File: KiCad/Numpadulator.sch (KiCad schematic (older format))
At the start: 1 part, among them U1 PRO_MICRO_C

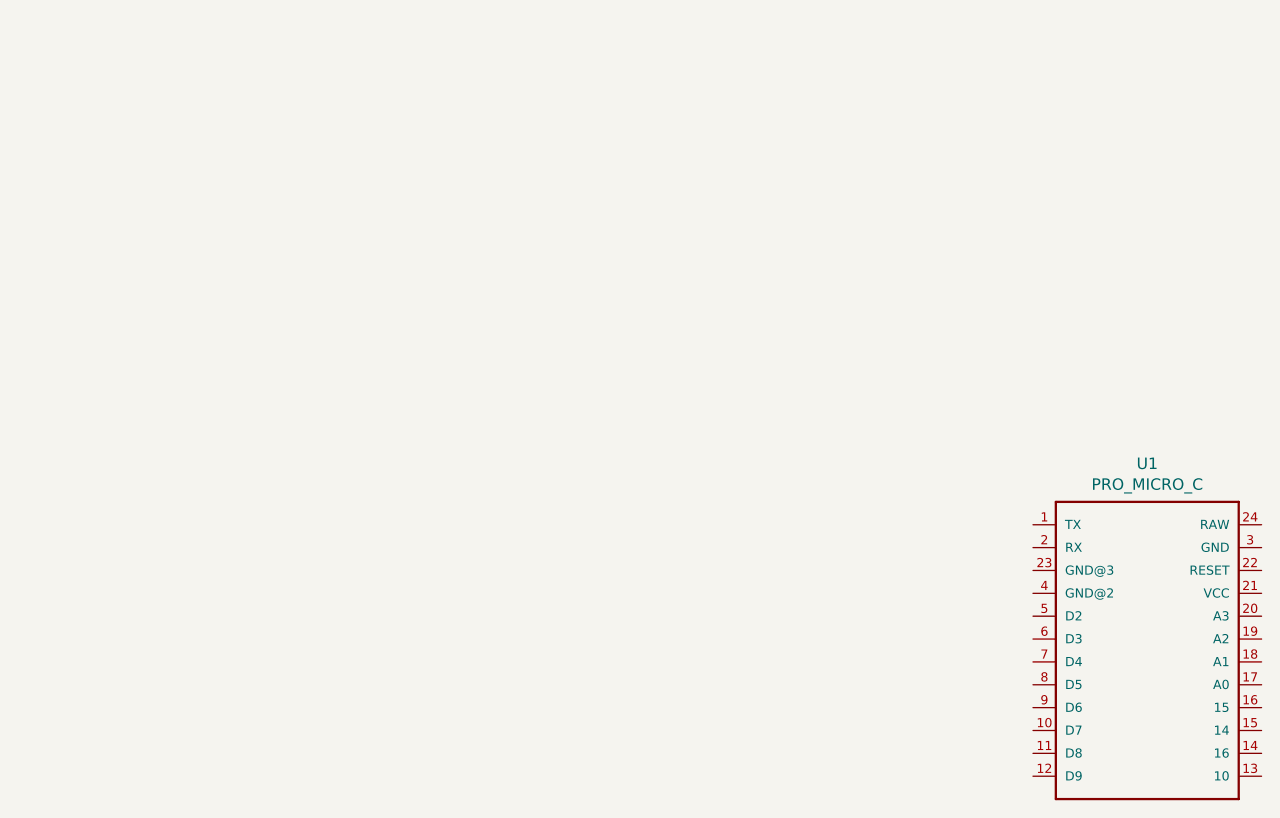
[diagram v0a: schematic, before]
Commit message: Dropped in RotEnc and hooked up OLED
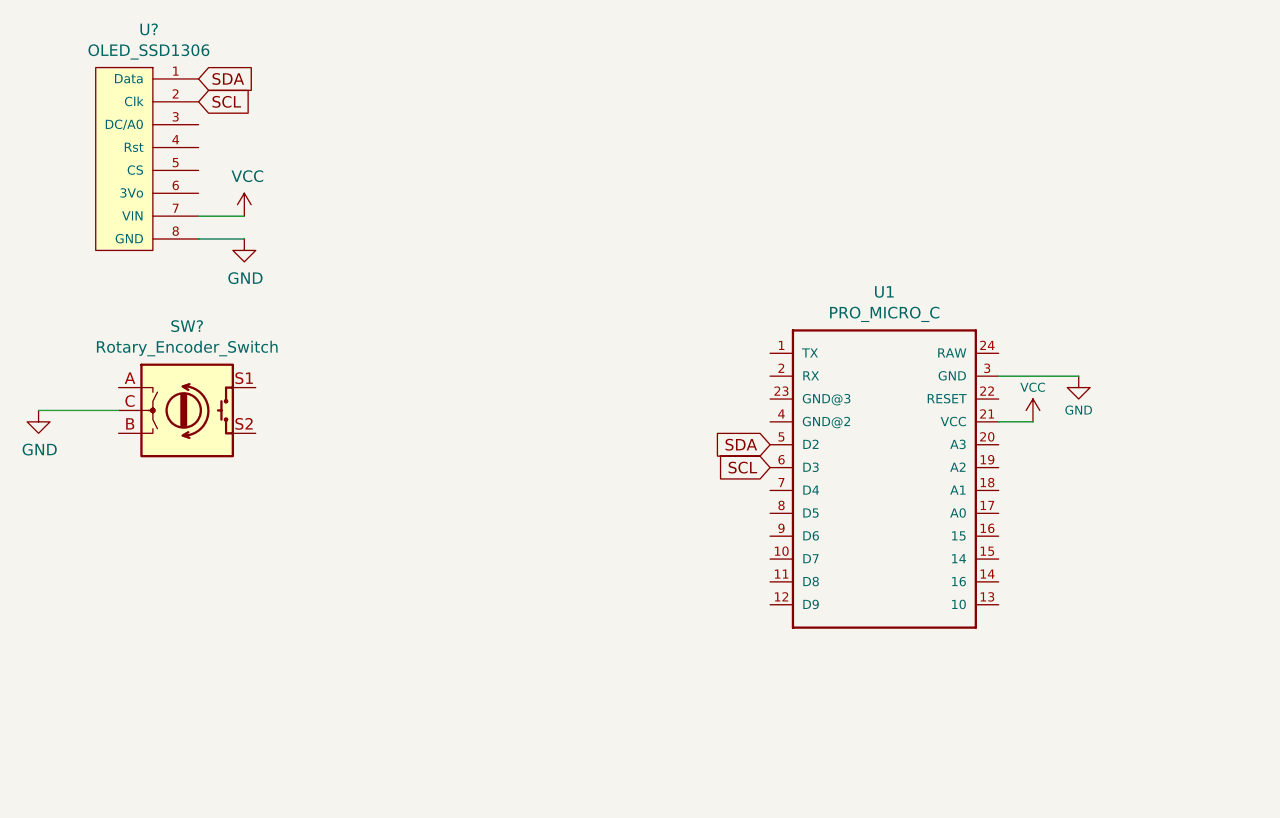
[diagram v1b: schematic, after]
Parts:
- added SW?: Rotary_Encoder_Switch, symbol Device:Rotary_Encoder_Switch
- added U?: OLED_SSD1306, symbol Custom_Library:OLED_SSD1306
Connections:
- net VCC: now reaches U1.21 (VCC)
- net VCC: now also U?.7 (VIN)
- net GND: now reaches U1.3 (GND)
- net GND: now also SW?.C, U?.8 (GND)
- net SDA: now reaches U1.5 (D2)
- net SDA: now also U?.1 (Data)
- net SCL: now reaches U1.6 (D3)
- net SCL: now also U?.2 (Clk)
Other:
- moved on the sheet: U1
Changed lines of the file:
@@
 L PRO_MICRO_C:PRO_MICRO_C U1
 U 1 1 5F1B84A1
-P 5600 3350
-F 0 "U1" H 5600 4117 50  0000 C CNN
-F 1 "PRO_MICRO_C" H 5600 4026 50  0000 C CNN
-F 2 "SparkFun-Boards:PRO_MICRO_C" H 5600 3350 50  0001 L BNN
-F 3 "" H 5600 3350 50  0001 C CNN
-	1    5600 3350
+P 4450 2600
+F 0 "U1" H 4450 3367 50  0000 C CNN
+F 1 "PRO_MICRO_C" H 4450 3276 50  0000 C CNN
+F 2 "SparkFun-Boards:PRO_MICRO_C" H 4450 2600 50  0001 L BNN
+F 3 "" H 4450 2600 50  0001 C CNN
+	1    4450 2600
 	1    0    0    -1
 $EndComp
+$Comp
+L Device:Rotary_Encoder_Switch SW?
+U 1 1 5F1D3156
+P 1400 2350
+F 0 "SW?" H 1400 2717 50  0000 C CNN
+F 1 "Rotary_Encoder_Switch" H 1400 2626 50  0000 C CNN
+F 2 "" H 1250 2510 50  0001 C CNN
+F 3 "~" H 1400 2610 50  0001 C CNN
+	1    1400 2350
+	1    0    0    -1
+$EndComp
+$Comp
+L Custom_Library:OLED_SSD1306 U?
+U 1 1 5F1EF454
+P 1100 1250
+F 0 "U?" V 535 1383 50  0000 C CNN
+F 1 "OLED_SSD1306" V 626 1383 50  0000 C CNN
+F 2 "" H 1150 1725 50  0001 C CNN
+F 3 "" H 1150 1725 50  0001 C CNN
+	1    1100 1250
+	0    1    1    0
+$EndComp
+Text GLabel 1450 900  2    50   Input ~ 0
+SDA
+Text GLabel 1450 1000 2    50   Input ~ 0
+SCL
+Text GLabel 3950 2500 0    50   Input ~ 0
+SDA
+Text GLabel 3950 2600 0    50   Input ~ 0
+SCL
+$Comp
+L power:VCC #PWR?
+U 1 1 5F1F5638
+P 1650 1500
+F 0 "#PWR?" H 1650 1350 50  0001 C CNN
+F 1 "VCC" H 1665 1673 50  0000 C CNN
+F 2 "" H 1650 1500 50  0001 C CNN
+F 3 "" H 1650 1500 50  0001 C CNN
+	1    1650 1500
+	1    0    0    -1
+$EndComp
+$Comp
+L power:GND #PWR?
+U 1 1 5F1F5EDF
+P 1650 1600
+F 0 "#PWR?" H 1650 1350 50  0001 C CNN
+F 1 "GND" H 1655 1427 50  0000 C CNN
+F 2 "" H 1650 1600 50  0001 C CNN
+F 3 "" H 1650 1600 50  0001 C CNN
+	1    1650 1600
+	1    0    0    -1
+$EndComp
+Wire Wire Line
+	1450 1500 1650 1500
+Wire Wire Line
+	1450 1600 1650 1600
+$Comp
+L power:VCC #PWR?
+U 1 1 5F1F629E
+P 5100 2400
+F 0 "#PWR?" H 5100 2250 50  0001 C CNN
+F 1 "VCC" H 5100 2550 39  0000 C CNN
+F 2 "" H 5100 2400 50  0001 C CNN
+F 3 "" H 5100 2400 50  0001 C CNN
+	1    5100 2400
+	1    0    0    -1
+$EndComp
+Wire Wire Line
+	4950 2400 5100 2400
+$Comp
+L power:GND #PWR?
+U 1 1 5F1F7964
+P 750 2350
+F 0 "#PWR?" H 750 2100 50  0001 C CNN
+F 1 "GND" H 755 2177 50  0000 C CNN
+F 2 "" H 750 2350 50  0001 C CNN
+F 3 "" H 750 2350 50  0001 C CNN
+	1    750  2350
+	1    0    0    -1
+$EndComp
+Wire Wire Line
+	1100 2350 750  2350
+$Comp
+L power:GND #PWR?
+U 1 1 5F1FE193
+P 5300 2200
+F 0 "#PWR?" H 5300 1950 50  0001 C CNN
+F 1 "GND" H 5300 2050 39  0000 C CNN
+F 2 "" H 5300 2200 50  0001 C CNN
+F 3 "" H 5300 2200 50  0001 C CNN
+	1    5300 2200
+	1    0    0    -1
+$EndComp
+Wire Wire Line
+	4950 2200 5300 2200
 $EndSCHEMATC

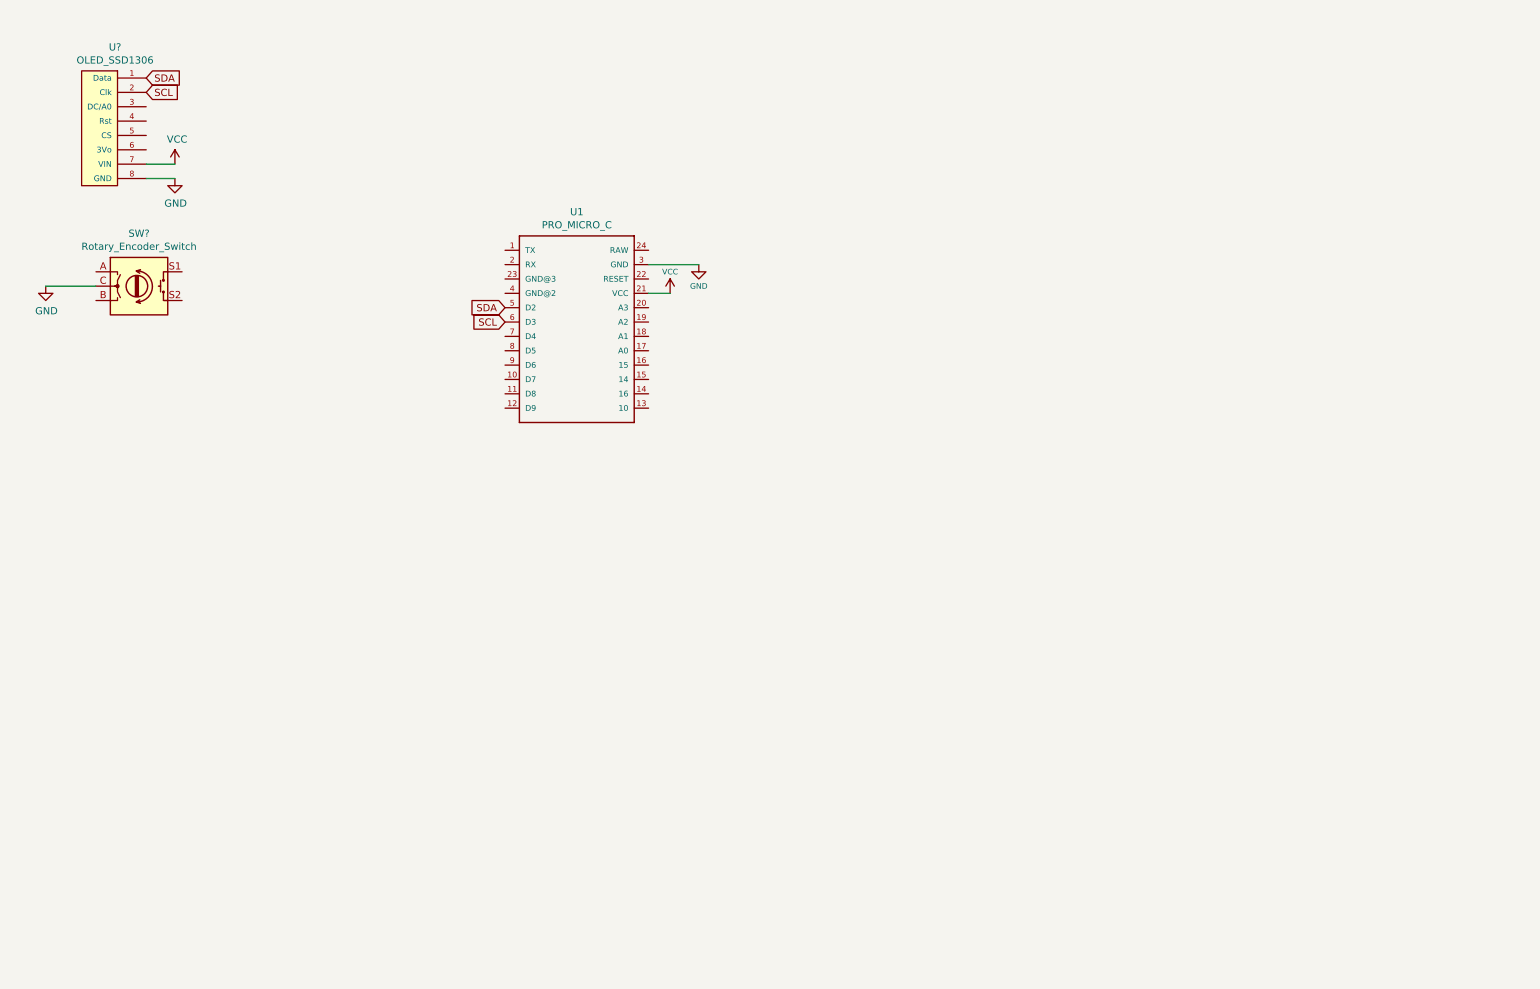
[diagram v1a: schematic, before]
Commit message: Added matrix w/o power
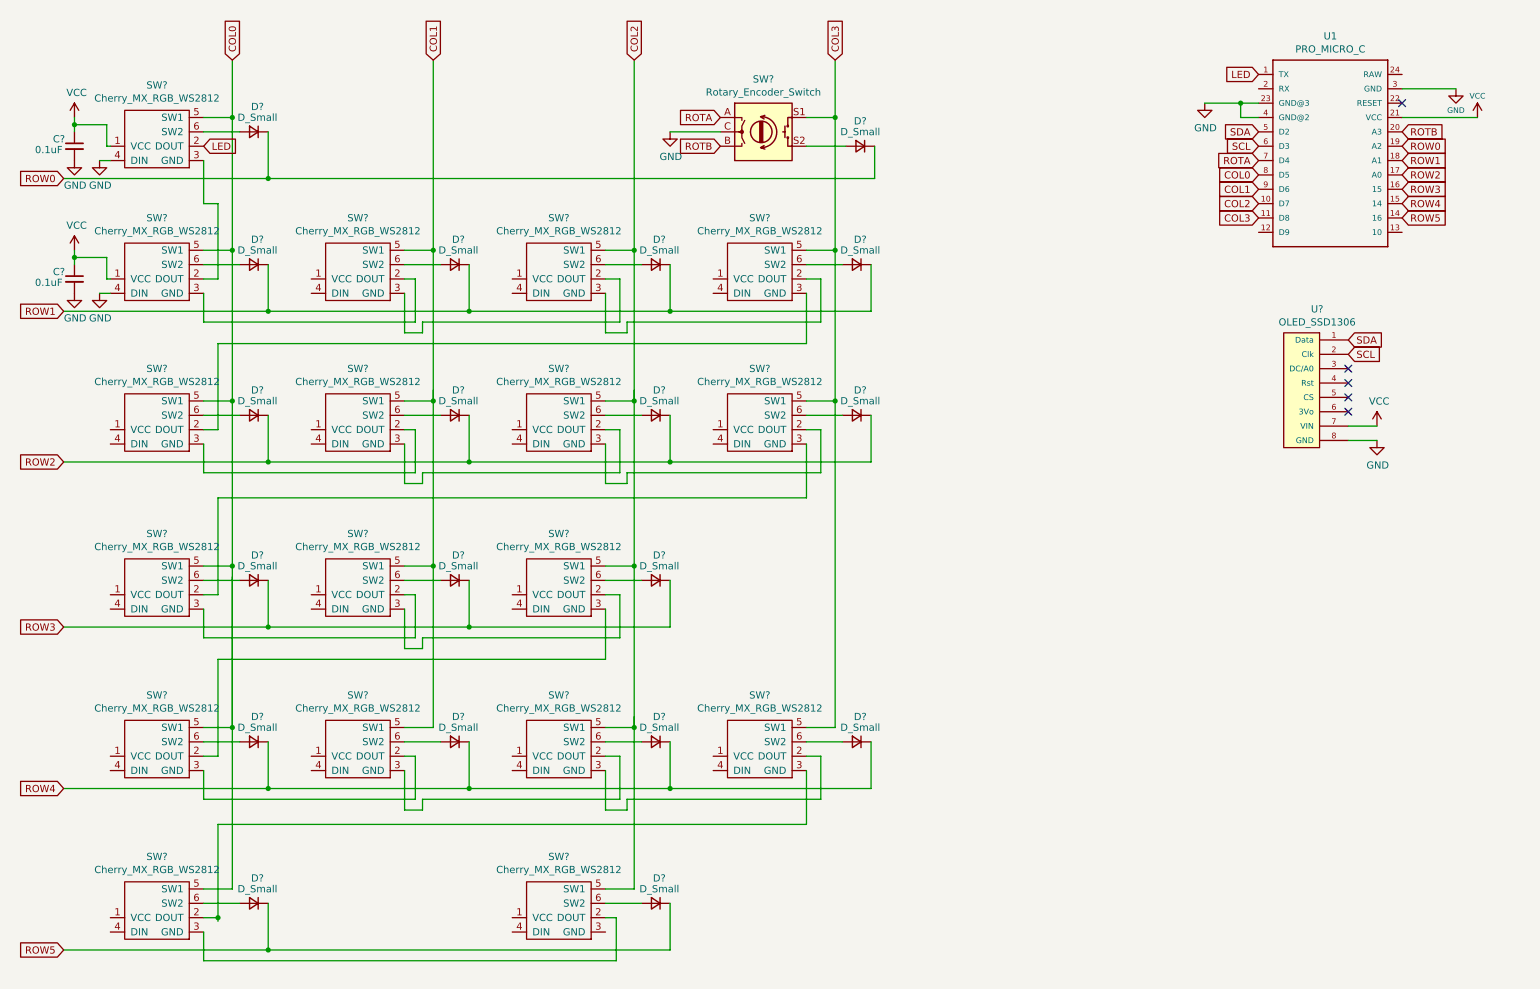
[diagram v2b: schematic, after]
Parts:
- added C? (x2): 0.1uF, symbol Device:C_Small
- added D? (x19): D_Small, symbol Device:D_Small
- added SW? (x18): Cherry_MX_RGB_WS2812, symbol Custom_Library:Cherry_MX_RGB_WS2812
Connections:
- net GND: now also U1.23 (GND@3), U1.4 (GND@2), C?.2, C?.2, SW?.4 (DIN), SW?.4 (DIN)
- net VCC: now also C?.1, C?.1, SW?.1 (VCC), SW?.1 (VCC)
- net LED: now reaches U1.1 (TX)
- net LED: now also SW?.2 (DOUT)
- net COL2: now reaches U1.10 (D7)
- net COL2: now also SW?.5 (SW1), SW?.5 (SW1), SW?.5 (SW1), SW?.5 (SW1), SW?.5 (SW1)
- net COL3: now reaches U1.11 (D8)
- net COL3: now also SW?.S1, SW?.5 (SW1), SW?.5 (SW1), SW?.5 (SW1)
- net ROW5: now reaches U1.14 (16)
- net ROW5: now also D?.1 (K), D?.1 (K)
- net ROW4: now reaches U1.15 (14)
- net ROW4: now also D?.1 (K), D?.1 (K), D?.1 (K), D?.1 (K)
- net ROW3: now reaches U1.16 (15)
- net ROW3: now also D?.1 (K), D?.1 (K), D?.1 (K)
- net ROW2: now reaches U1.17 (A0)
- net ROW2: now also D?.1 (K), D?.1 (K), D?.1 (K), D?.1 (K)
- net ROW1: now reaches U1.18 (A1)
- net ROW1: now also D?.1 (K), D?.1 (K), D?.1 (K), D?.1 (K)
- net ROW0: now reaches U1.19 (A2)
- net ROW0: now also D?.1 (K), D?.1 (K)
- net ROTB: now reaches U1.20 (A3)
- net ROTB: now also SW?.B
- net ROTA: now reaches U1.7 (D4)
- net ROTA: now also SW?.A
- net COL0: now reaches U1.8 (D5)
- net COL0: now also SW?.5 (SW1), SW?.5 (SW1), SW?.5 (SW1), SW?.5 (SW1), SW?.5 (SW1), SW?.5 (SW1)
- net COL1: now reaches U1.9 (D6)
- net COL1: now also SW?.5 (SW1), SW?.5 (SW1), SW?.5 (SW1), SW?.5 (SW1)
- net at SW?.S2: now also D?.2 (A)
- new net: SW?.2 (DOUT), SW?.3 (GND) (x17)
- new net: D?.2 (A), SW?.6 (SW2) (x18)
- no-connect marks 0 -> 5
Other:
- moved on the sheet: SW?, U1, U?

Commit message: Started to make look better
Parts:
- added C?: 0.1uF, symbol Device:C_Small
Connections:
- wire segments 203 -> 201
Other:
- moved on the sheet: D?, SW?

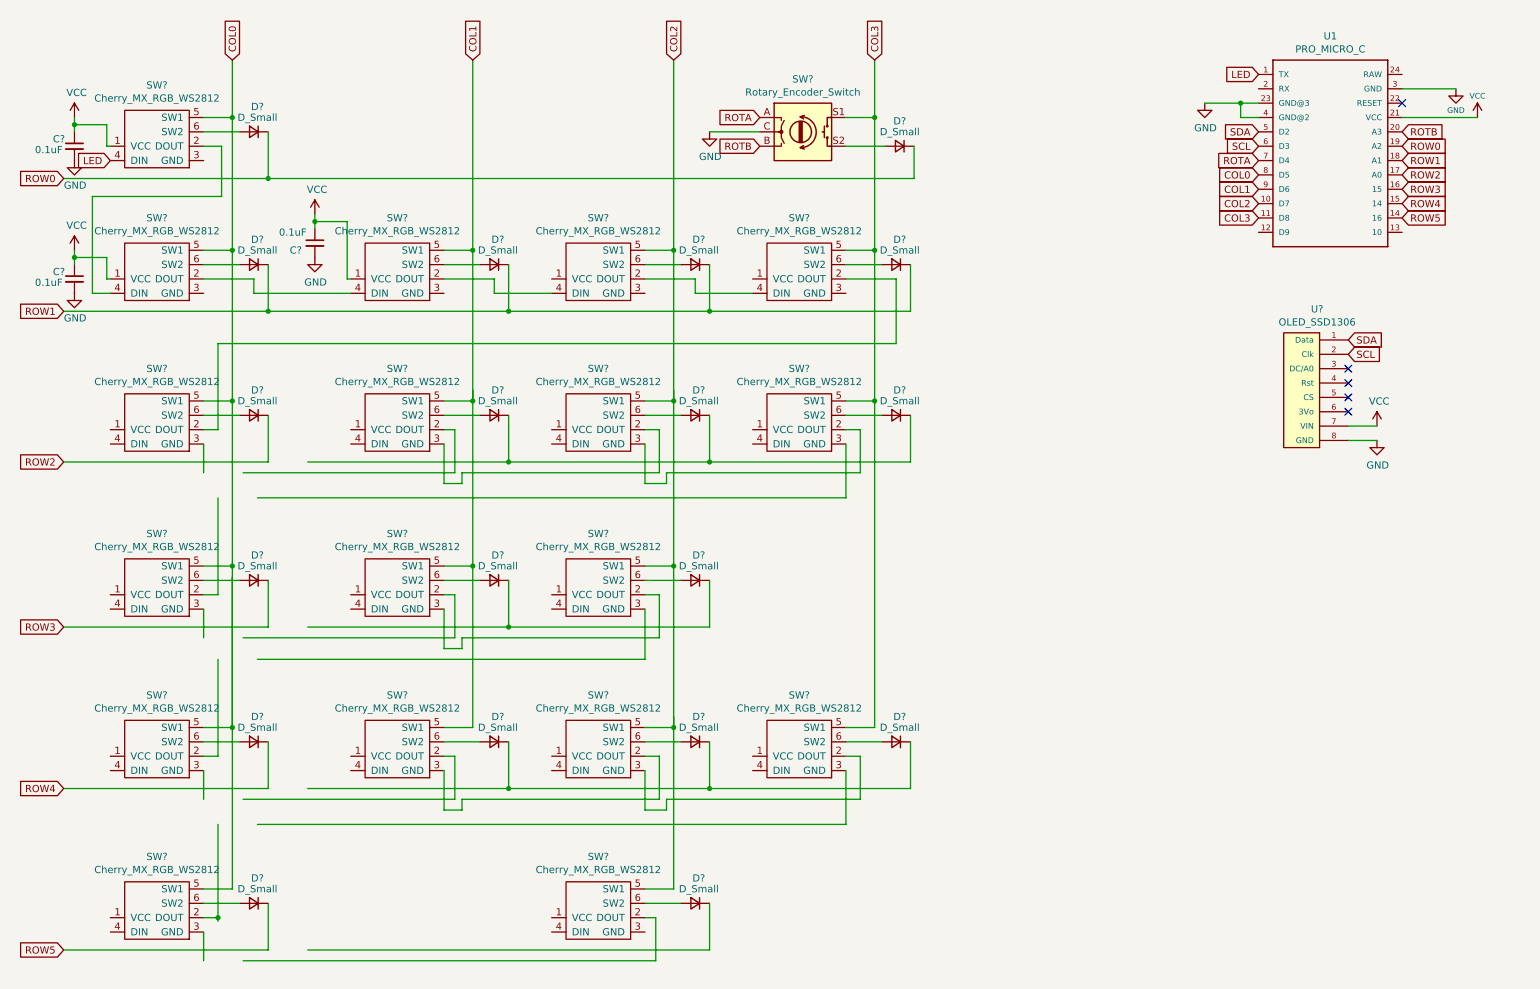
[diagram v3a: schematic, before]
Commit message: Reworked main matrix schem
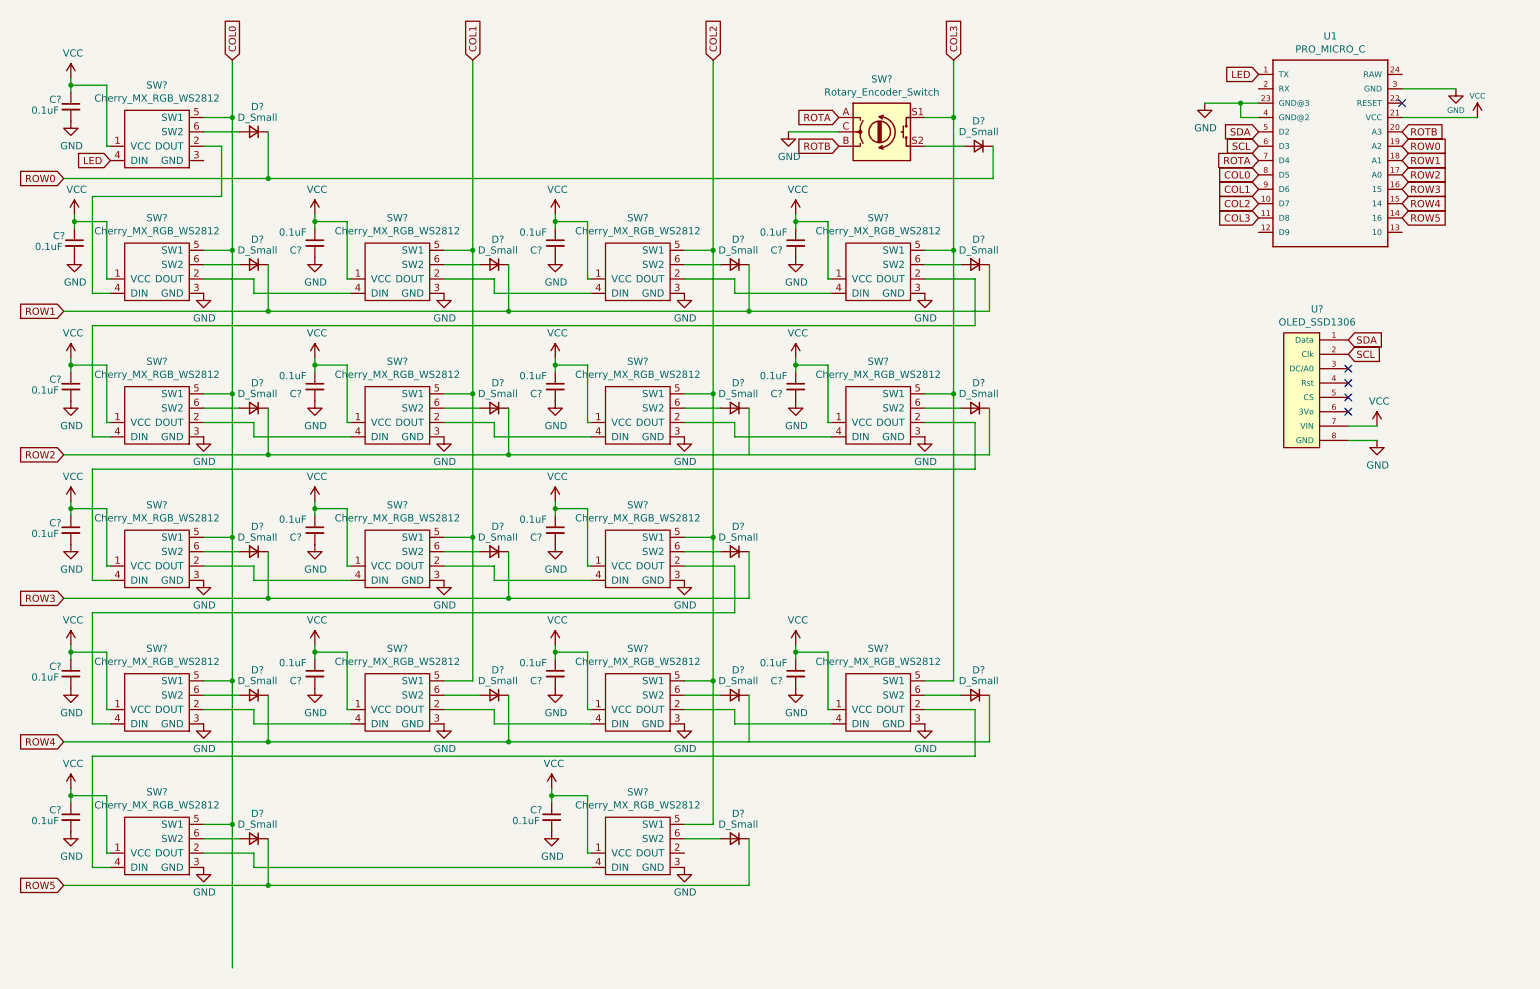
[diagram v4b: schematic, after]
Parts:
- removed D? (x15): D_Small, symbol Device:D_Small
- removed SW? (x15): Cherry_MX_RGB_WS2812, symbol Custom_Library:Cherry_MX_RGB_WS2812
- added C? (x15): 0.1uF, symbol Device:C_Small
- added D? (x15): D_Small, symbol Device:D_Small
- added SW? (x15): Cherry_MX_RGB_WS2812, symbol Custom_Library:Cherry_MX_RGB_WS2812
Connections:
- wire segments 201 -> 254
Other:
- moved on the sheet: C?, D?, SW?

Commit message: A little cleanup
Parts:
- gave numbers to parts that had none: 57
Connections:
- net GND: now also SW1.3 (GND)
- no-connect marks 5 -> 9
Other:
- note added: "Numpadulator"
- note added: "These decoupling caps on LEDs\nare recomended by the datasheet"
